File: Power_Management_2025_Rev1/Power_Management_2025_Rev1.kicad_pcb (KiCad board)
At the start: 2 copper layers, 213.1 x 179.3 mm, 100 parts, among them J1 RJ45_LED_Shielded, Q1 BSS138, Q2 IPB180N10S4-02, Q3 IPB180N10S4-02, Q4 IPB180N10S4-02, U1 Teensy4.1_DEV-16771, U10 LT1910, U11 LT1910, U12 PKE3316ZPI, U13 PKE3316ZPI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

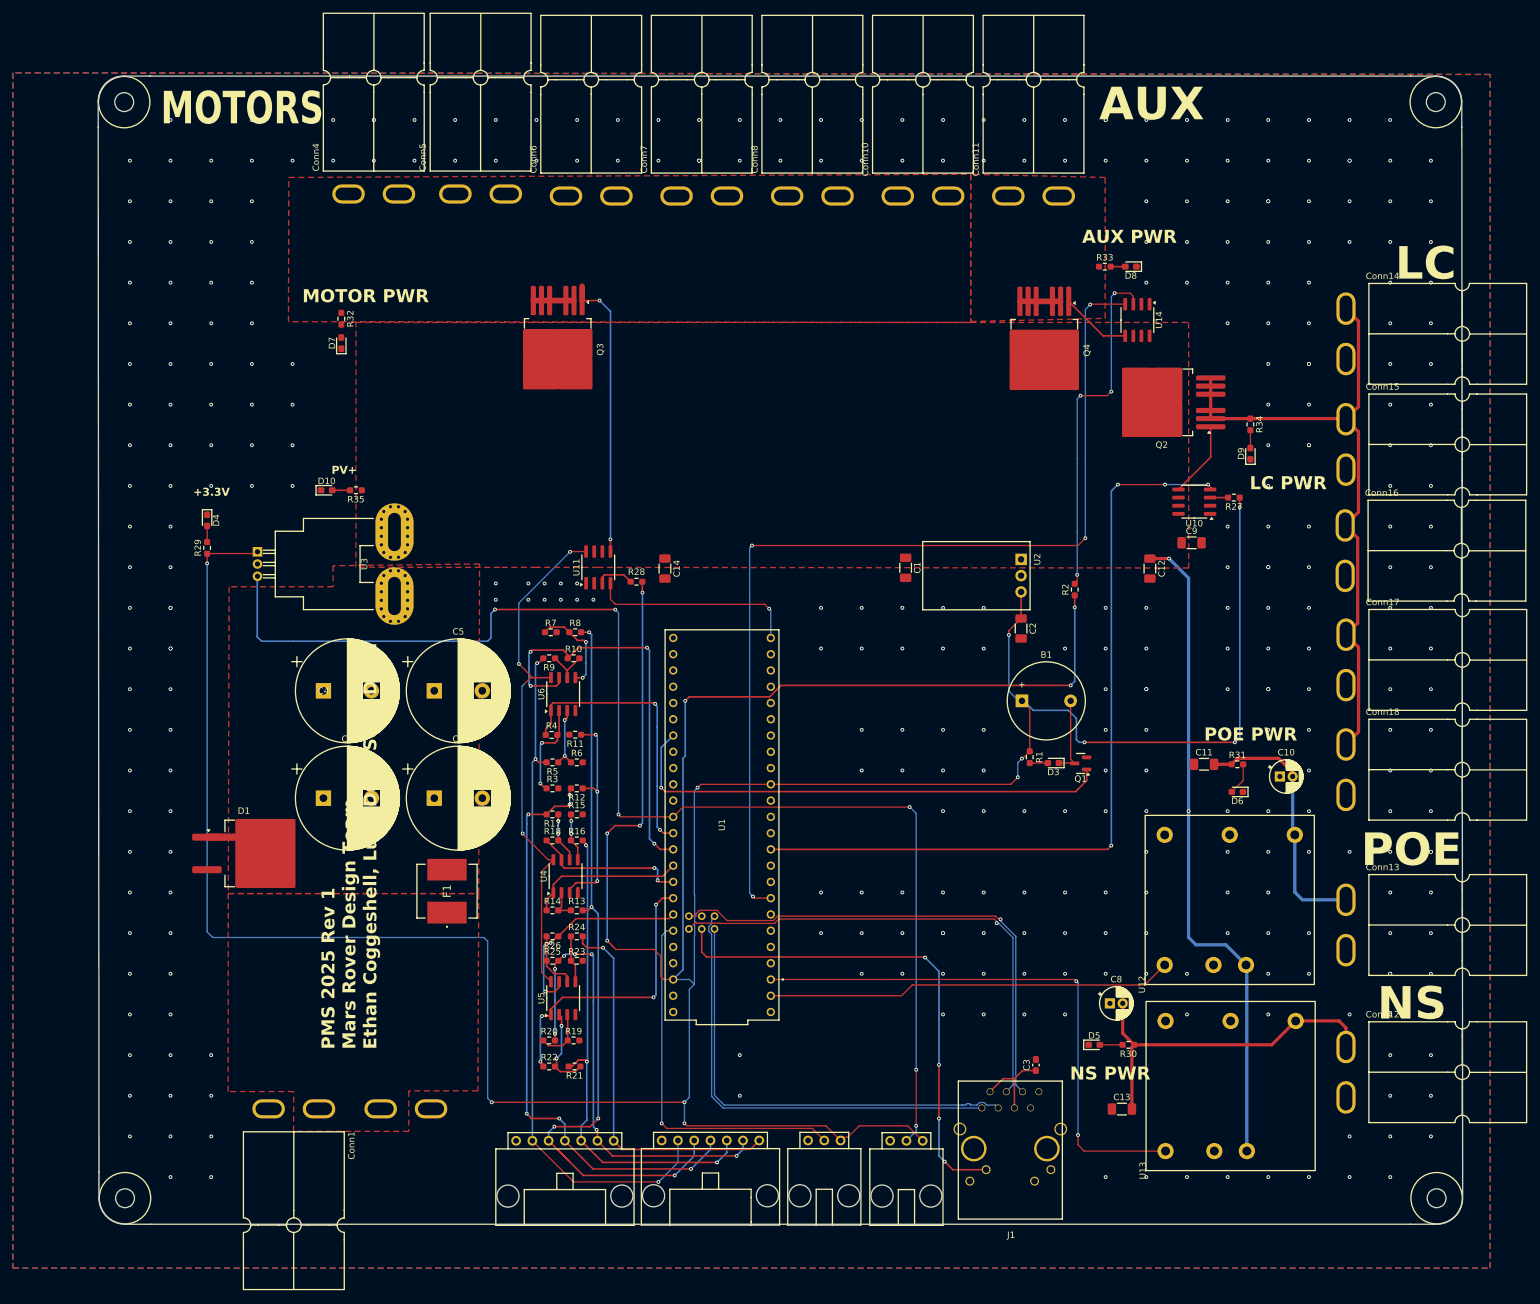
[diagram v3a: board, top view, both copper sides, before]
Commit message: retraced opamp circuit to be more symetric
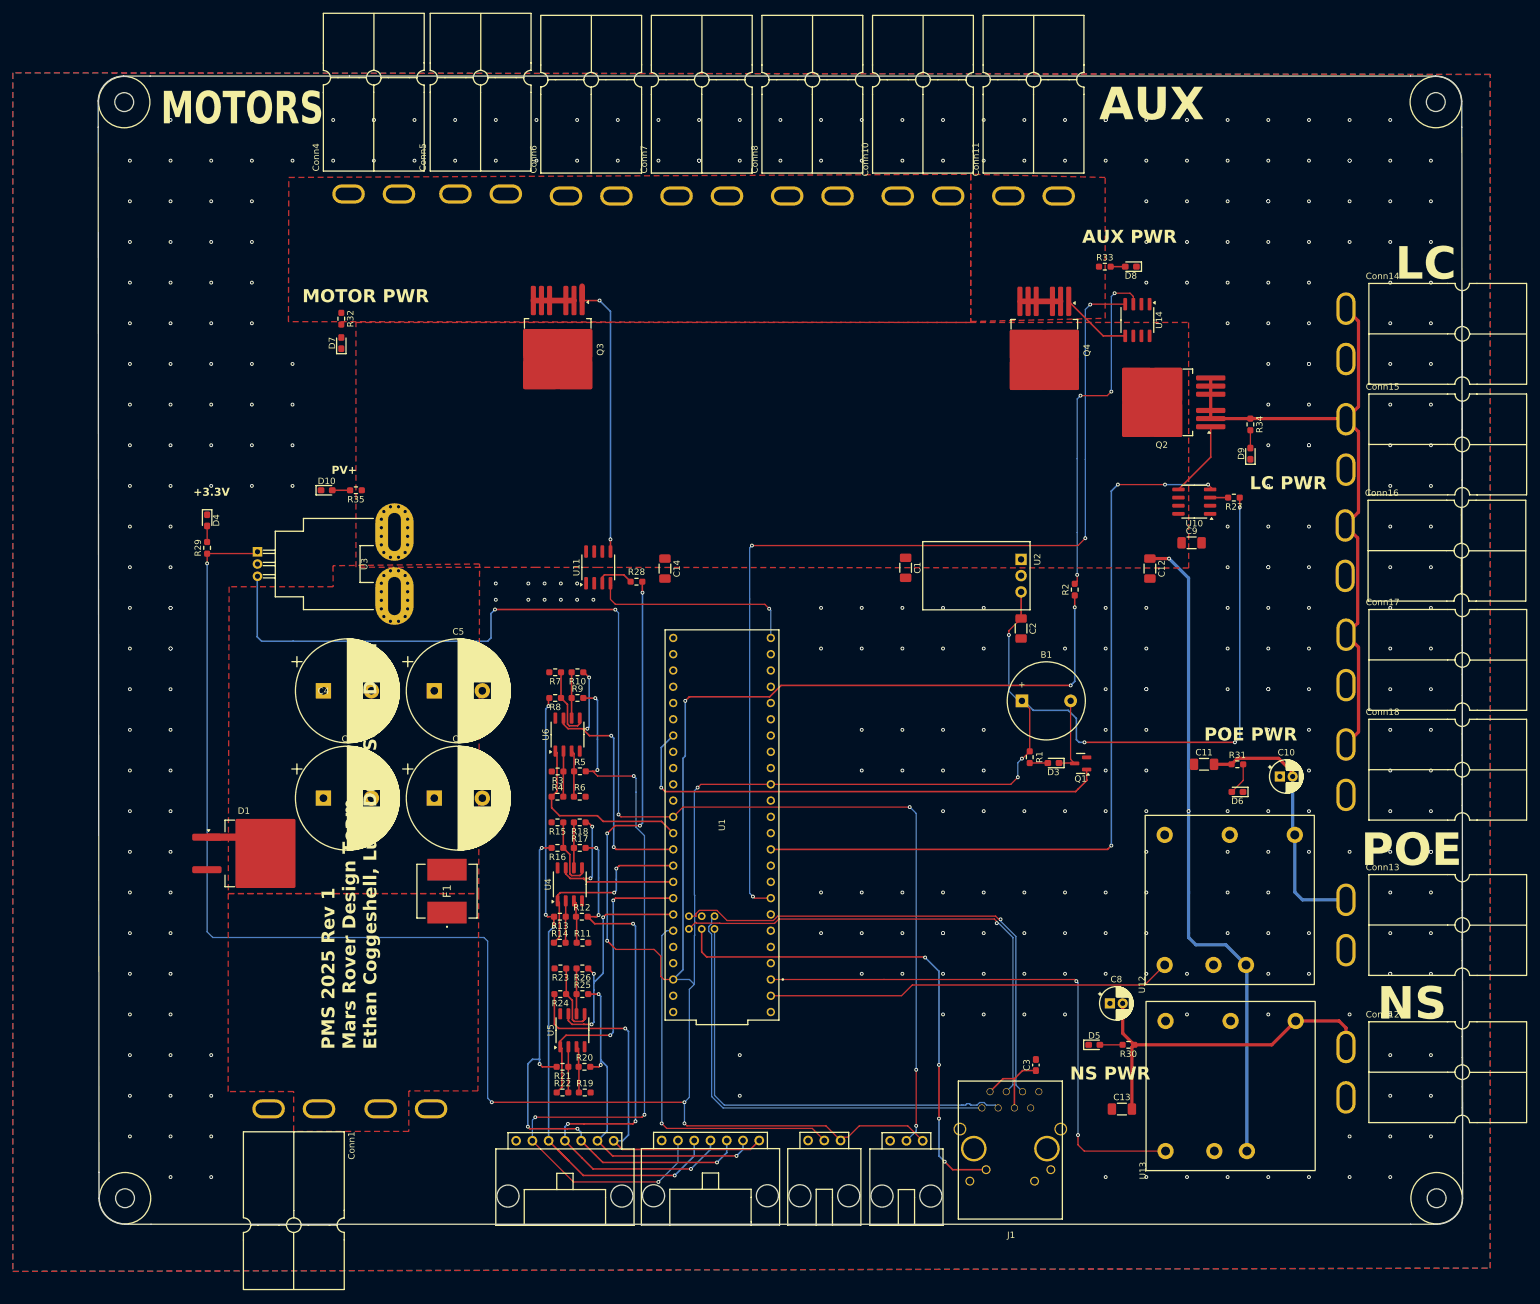
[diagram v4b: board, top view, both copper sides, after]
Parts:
- moved R11 32.5 mm to (102.4, 147.5), turned to 0 degrees
- moved R12 20.1 mm to (102.3, 143.5), turned to 0 degrees
- moved R8 10.7 mm to (98.2, 109.3), turned to 180 degrees
- moved R4 9.69 mm to (98.5, 124.7)
- moved R24 9.38 mm to (99.0, 155.6), turned to 180 degrees
- moved R19 8.31 mm to (102.8, 170.9)
- moved R9 7.61 mm to (101.7, 109.3), turned to 0 degrees
- moved R25 7.00 mm to (102.4, 155.6)
- moved R20 6.88 mm to (102.7, 166.9)
- moved R26 6.85 mm to (102.4, 151.6)
- moved R17 6.75 mm to (102.0, 132.7), turned to 0 degrees
- moved U6 6.36 mm to (100.1, 115.0)
- moved R7 6.29 mm to (98.2, 105.3), turned to 180 degrees
- moved R6 5.38 mm to (102.0, 124.7)
- moved U5 5.21 mm to (100.9, 161.2)
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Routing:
- net IP-: track 187.8 -> 103.3 mm, vias 5 -> 2
- net Net-(U4A-+): track 33.1 -> 6.72 mm, vias 3 -> 0
- net CELL5: track 73.3 -> 53.8 mm, vias 7 -> 3
- net CELL_SENSE_2: track 65.3 -> 46.3 mm
- net CELL2: track 123.0 -> 104.5 mm, vias 5 -> 4
- net CELL1: track 108.4 -> 126.8 mm, vias 3 -> 6
- net CELL_SENSE_1: track 43.8 -> 29.9 mm, vias 2 -> 0
- net CELL4: track 78.5 -> 86.9 mm, vias 3 -> 5
- net Net-(U6A--): track 15.1 -> 7.14 mm, vias 2 -> 0
- net Net-(U5A--): track 13.3 -> 7.15 mm, vias 2 -> 0
- net CELL_SENSE_3: track 24.4 -> 29.9 mm, vias 0 -> 2
- net CELL_SENSE_4: track 24.3 -> 29.5 mm
- net Net-(U5B-+): track 7.36 -> 11.7 mm
- net Net-(U4B-+): track 7.56 -> 11.5 mm, vias 2 -> 0
- net CELL_SENSE_6: track 32.8 -> 36.1 mm, vias 2 -> 3
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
